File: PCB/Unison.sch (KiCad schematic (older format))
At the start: 258 parts, among them J1 USB4085-GF-A_REVA, U1 ATmega32U4-AU, Y1 16MHz

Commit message: Update: 回路図、PCB。ロータリーエンコーダをマウント穴付きのEC11Kタイプに対応。
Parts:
- SW_RE1, SW_RE2, SW_RE3, SW_RE4, SW_RE5: footprint Rotary_Encoder:RotaryEncoder_Alps_EC11E-Switch_Vertical_H20mm -> ukiha:RotaryEncoder_Alps_EC11K-Switch_Vertical_H20mm
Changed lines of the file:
@@
 F 0 "SW_RE1" H 1150 11267 50  0000 C CNN
 F 1 "Rotary_Encoder_Switch" H 1150 11176 50  0000 C CNN
-F 2 "Rotary_Encoder:RotaryEncoder_Alps_EC11E-Switch_Vertical_H20mm" H 1000 11060 50  0001 C CNN
+F 2 "ukiha:RotaryEncoder_Alps_EC11K-Switch_Vertical_H20mm" H 1000 11060 50  0001 C CNN
 F 3 "~" H 1150 11160 50  0001 C CNN
 	1    1150 10900
@@
 F 0 "SW_RE2" H 2525 11267 50  0000 C CNN
 F 1 "Rotary_Encoder_Switch" H 2525 11176 50  0000 C CNN
-F 2 "Rotary_Encoder:RotaryEncoder_Alps_EC11E-Switch_Vertical_H20mm" H 2375 11060 50  0001 C CNN
+F 2 "ukiha:RotaryEncoder_Alps_EC11K-Switch_Vertical_H20mm" H 2375 11060 50  0001 C CNN
 F 3 "~" H 2525 11160 50  0001 C CNN
 	1    2525 10900
@@
 F 0 "SW_RE3" H 4150 11267 50  0000 C CNN
 F 1 "Rotary_Encoder_Switch" H 4150 11176 50  0000 C CNN
-F 2 "Rotary_Encoder:RotaryEncoder_Alps_EC11E-Switch_Vertical_H20mm" H 4000 11060 50  0001 C CNN
+F 2 "ukiha:RotaryEncoder_Alps_EC11K-Switch_Vertical_H20mm" H 4000 11060 50  0001 C CNN
 F 3 "~" H 4150 11160 50  0001 C CNN
 	1    4150 10900
@@
 F 0 "SW_RE4" H 5550 11267 50  0000 C CNN
 F 1 "Rotary_Encoder_Switch" H 5550 11176 50  0000 C CNN
-F 2 "Rotary_Encoder:RotaryEncoder_Alps_EC11E-Switch_Vertical_H20mm" H 5400 11060 50  0001 C CNN
+F 2 "ukiha:RotaryEncoder_Alps_EC11K-Switch_Vertical_H20mm" H 5400 11060 50  0001 C CNN
 F 3 "~" H 5550 11160 50  0001 C CNN
 	1    5550 10900
@@
 F 0 "SW_RE5" H 6950 11267 50  0000 C CNN
 F 1 "Rotary_Encoder_Switch" H 6950 11176 50  0000 C CNN
-F 2 "Rotary_Encoder:RotaryEncoder_Alps_EC11E-Switch_Vertical_H20mm" H 6800 11060 50  0001 C CNN
+F 2 "ukiha:RotaryEncoder_Alps_EC11K-Switch_Vertical_H20mm" H 6800 11060 50  0001 C CNN
 F 3 "~" H 6950 11160 50  0001 C CNN
 	1    6950 10900

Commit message: Update: ポテンションメータを追加。配線未完了。
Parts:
- added RV1: R_POT, Potentiometer_THT:Potentiometer_Bourns_PTA3043_Single_Slide, symbol Device:R_POT
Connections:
- net +5V: now also RV1.1
- net GND: now also RV1.3
- net AUDIO1 renamed AUDIO
- net AUDIO: no longer U1.30 (PB6)
- new net ANALOG: RV1.2, U1.30 (PB6)
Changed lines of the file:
@@
 $EndComp
 Text GLabel 1450 9925 2    50   Input ~ 0
-AUDIO1
+AUDIO
 $Comp
 L power:GND #PWR01
@@
 Wire Wire Line
 	925  10025 925  10225
-Text GLabel 15300 2725 2    50   Input ~ 0
-AUDIO1
+Text GLabel 15300 3025 2    50   Input ~ 0
+AUDIO
 Connection ~ 4800 6575
 Wire Wire Line
@@
 	1    0    0    -1
 $EndComp
-Text GLabel 15300 3025 2    50   Input ~ 0
-AUDIO2[Reserve]
+Text GLabel 15300 2725 2    50   Input ~ 0
+ANALOG
 Connection ~ 1075 10225
 Wire Wire Line
@@
 Text GLabel 11050 2650 1    50   Input ~ 0
 RE5_2
-Text GLabel 1450 9775 2    50   Input ~ 0
-AUDIO2[Reserve]
-Wire Wire Line
-	1375 9925 1400 9925
-Wire Wire Line
-	1450 9775 1400 9775
-Connection ~ 1400 9925
-Wire Wire Line
-	1400 9925 1450 9925
 $Comp
 L power:GND #PWR029
@@
 	9350 9925 9825 9925
 Wire Wire Line
-	1400 9775 1400 9925
-Wire Wire Line
 	9825 9725 9825 9925
 Connection ~ 9825 9925
@@
 Wire Wire Line
 	10225 4575 10400 4575
+Wire Wire Line
+	1375 9925 1450 9925
+$Comp
+L Device:R_POT RV1
+U 1 1 600D2738
+P 2550 9925
+F 0 "RV1" H 2481 9971 50  0000 R CNN
+F 1 "R_POT" H 2481 9880 50  0000 R CNN
+F 2 "Potentiometer_THT:Potentiometer_Bourns_PTA3043_Single_Slide" H 2550 9925 50  0001 C CNN
+F 3 "~" H 2550 9925 50  0001 C CNN
+	1    2550 9925
+	1    0    0    -1
+$EndComp
+Text GLabel 2700 9925 2    50   Input ~ 0
+ANALOG
+$Comp
+L power:GND #PWR010
+U 1 1 6012B75D
+P 2550 10075
+F 0 "#PWR010" H 2550 9825 50  0001 C CNN
+F 1 "GND" H 2555 9902 50  0000 C CNN
+F 2 "" H 2550 10075 50  0001 C CNN
+F 3 "" H 2550 10075 50  0001 C CNN
+	1    2550 10075
+	1    0    0    -1
+$EndComp
+$Comp
+L power:+5V #PWR09
+U 1 1 60184491
+P 2550 9775
+F 0 "#PWR09" H 2550 9625 50  0001 C CNN
+F 1 "+5V" H 2565 9948 50  0000 C CNN
+F 2 "" H 2550 9775 50  0001 C CNN
+F 3 "" H 2550 9775 50  0001 C CNN
+	1    2550 9775
+	1    0    0    -1
+$EndComp
 $EndSCHEMATC

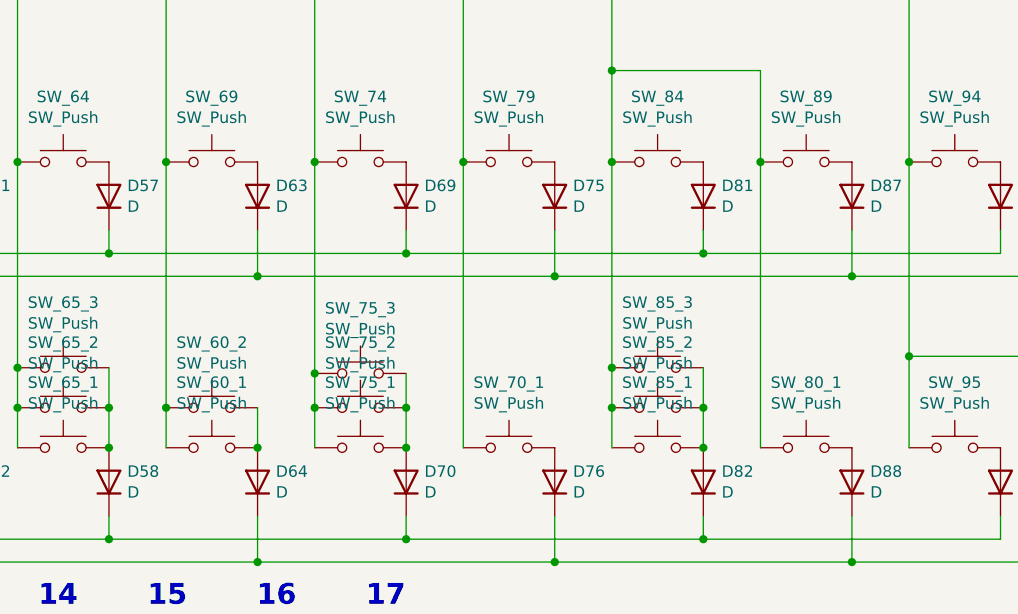
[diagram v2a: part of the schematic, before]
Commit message: Update: 右手親指Modに3キー追加。
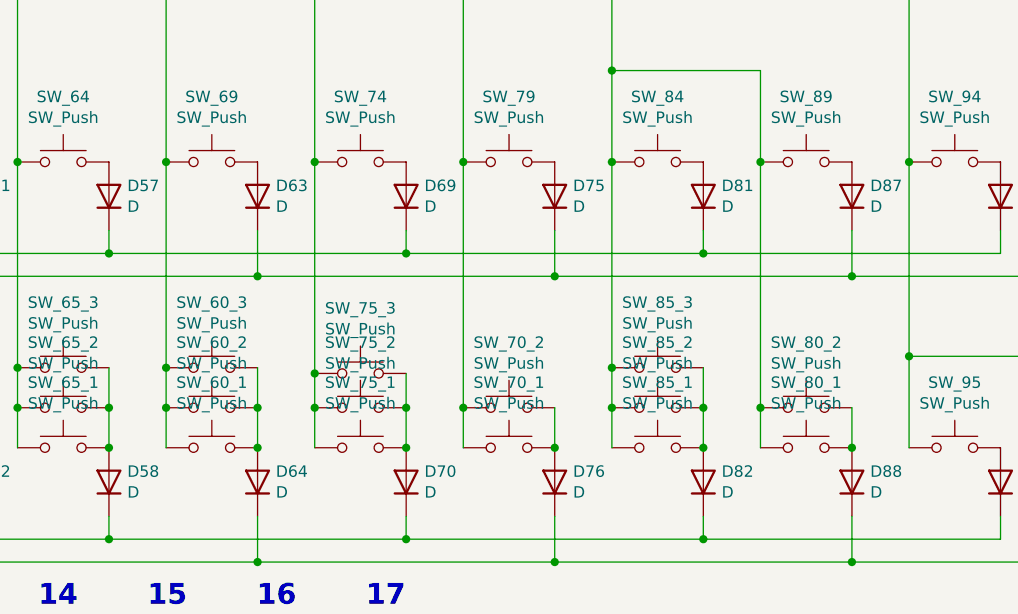
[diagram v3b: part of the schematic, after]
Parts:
- added SW_60_3: SW_Push, ukiha:CherryMX_MidHeight_16mm_rev2_2u_guide, symbol Switch:SW_Push
- added SW_70_2, SW_80_2: SW_Push, ukiha:CherryMX_MidHeight_16mm_rev2_1.5u_guide, symbol Switch:SW_Push
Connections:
- net RE2_1: now also SW_60_3.1
- net RE3_1: now also SW_70_2.1
- net RE4_1: now also SW_80_2.1
- net at D76.2 (A), SW_70_1.2: now also SW_70_2.2
- net at D88.2 (A), SW_80_1.2: now also SW_80_2.2
- net at D64.2 (A), SW_60_1.2, SW_60_2.2: now also SW_60_3.2
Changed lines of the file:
@@
 	4800 7225 4800 7825
 Wire Wire Line
-	7400 6575 7400 7650
+	7400 6575 7400 7475
 Wire Wire Line
 	8050 6575 8050 7500
 Wire Wire Line
-	8700 6575 8700 7825
+	8700 6575 8700 7650
 Wire Wire Line
 	9350 6575 9350 7475
 Wire Wire Line
-	10000 6575 10000 7825
+	10000 6575 10000 7650
 Wire Wire Line
 	2200 6575 2200 7625
@@
 	1    0    0    -1
 $EndComp
+$Comp
+L Switch:SW_Push SW_80_2
+U 1 1 601AB361
+P 10200 7650
+F 0 "SW_80_2" H 10200 7935 50  0000 C CNN
+F 1 "SW_Push" H 10200 7844 50  0000 C CNN
+F 2 "ukiha:CherryMX_MidHeight_16mm_rev2_1.5u_guide" H 10200 7850 50  0001 C CNN
+F 3 "~" H 10200 7850 50  0001 C CNN
+	1    10200 7650
+	1    0    0    -1
+$EndComp
+Connection ~ 10000 7650
+Wire Wire Line
+	10000 7650 10000 7825
+Wire Wire Line
+	10400 7650 10400 7825
+Connection ~ 10400 7825
+$Comp
+L Switch:SW_Push SW_70_2
+U 1 1 6026A20D
+P 8900 7650
+F 0 "SW_70_2" H 8900 7935 50  0000 C CNN
+F 1 "SW_Push" H 8900 7844 50  0000 C CNN
+F 2 "ukiha:CherryMX_MidHeight_16mm_rev2_1.5u_guide" H 8900 7850 50  0001 C CNN
+F 3 "~" H 8900 7850 50  0001 C CNN
+	1    8900 7650
+	1    0    0    -1
+$EndComp
+Connection ~ 8700 7650
+Wire Wire Line
+	8700 7650 8700 7825
+Wire Wire Line
+	9100 7650 9100 7825
+Connection ~ 9100 7825
+$Comp
+L Switch:SW_Push SW_60_3
+U 1 1 6032DF0B
+P 7600 7475
+F 0 "SW_60_3" H 7600 7760 50  0000 C CNN
+F 1 "SW_Push" H 7600 7669 50  0000 C CNN
+F 2 "ukiha:CherryMX_MidHeight_16mm_rev2_2u_guide" H 7600 7675 50  0001 C CNN
+F 3 "~" H 7600 7675 50  0001 C CNN
+	1    7600 7475
+	1    0    0    -1
+$EndComp
+Connection ~ 7400 7475
+Wire Wire Line
+	7400 7475 7400 7650
+Wire Wire Line
+	7800 7475 7800 7650
+Connection ~ 7800 7650
 $EndSCHEMATC

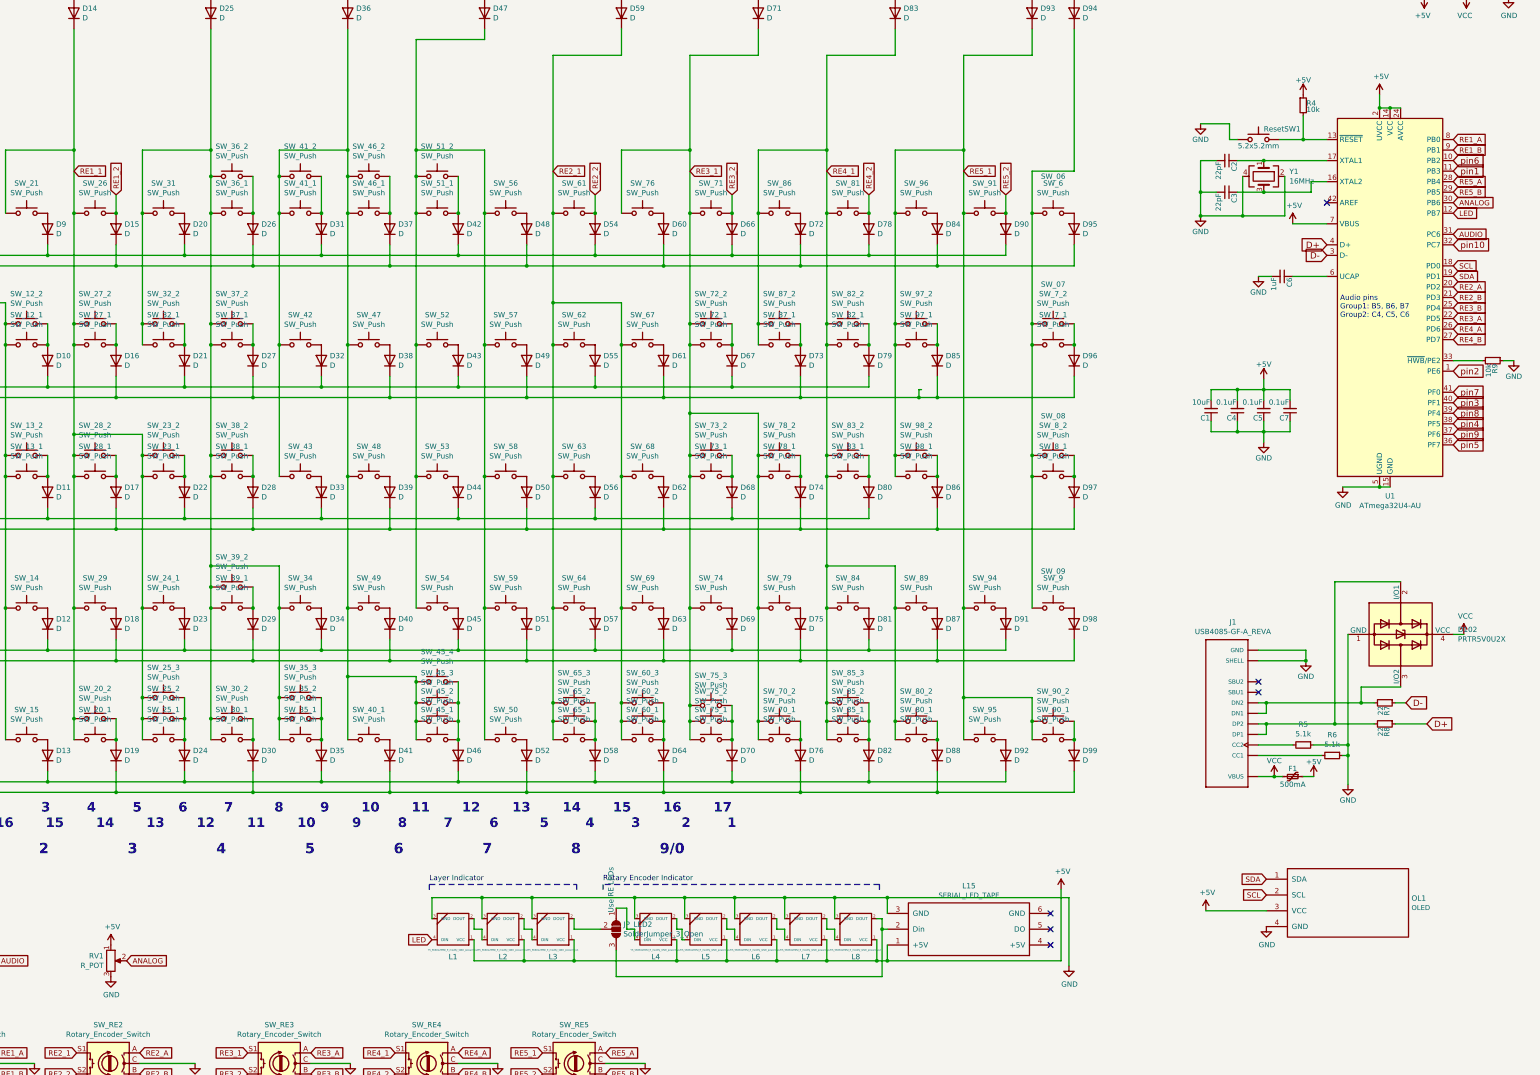
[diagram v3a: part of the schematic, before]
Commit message: Update: OLED, ポテンションメーター廃止。ICSPとI2Cをピンヘッダで用意。
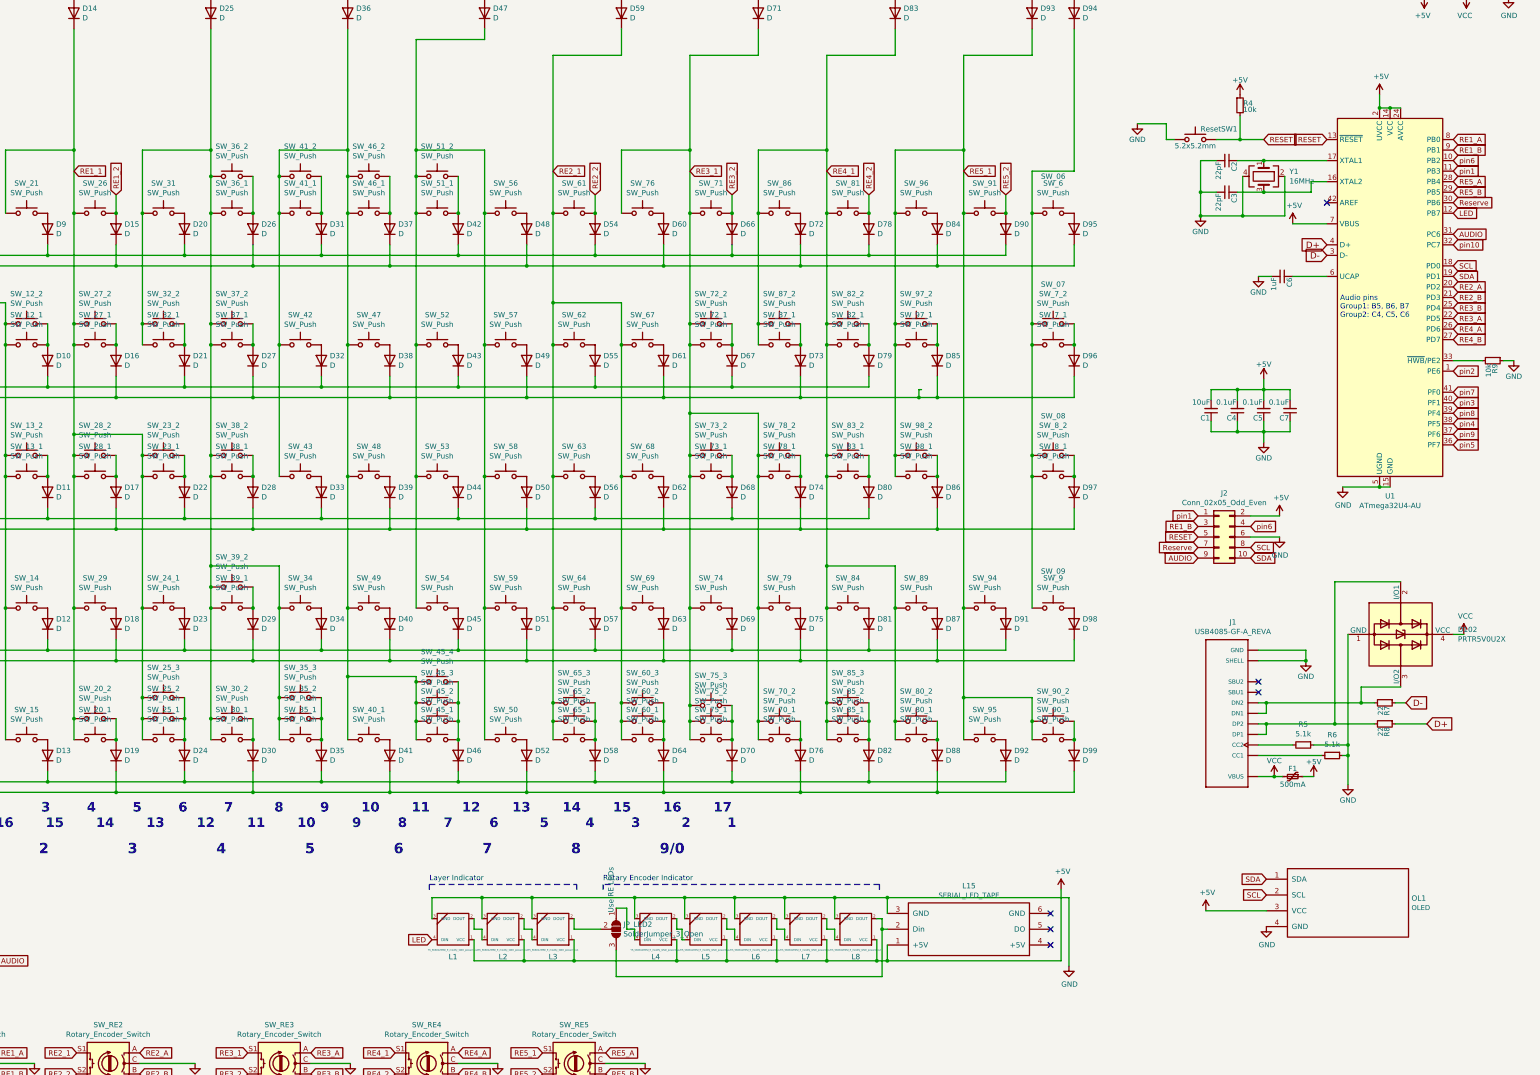
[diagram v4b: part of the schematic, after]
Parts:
- removed RV1: R_POT, Potentiometer_THT:Potentiometer_Bourns_PTA3043_Single_Slide, symbol Device:R_POT
- added J2: Conn_02x05_Odd_Even, Connector_PinHeader_2.54mm:PinHeader_2x05_P2.54mm_Vertical, symbol Connector_Generic:Conn_02x05_Odd_Even
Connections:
- net +5V: now also J2.2 (Pin_2)
- net AUDIO: now also J2.9 (Pin_9)
- net GND: now also J2.6 (Pin_6)
- net RE1_B: now also J2.3 (Pin_3)
- net SCL: now also J2.8 (Pin_8)
- net SDA: now also J2.10 (Pin_10)
- net pin1: now also J2.1 (Pin_1)
- net pin6: now also J2.4 (Pin_4)
- net RESET: now reaches R4.2, ResetSW1.2, U1.13 (~RESET)
- net RESET: now also J2.5 (Pin_5)
- net ANALOG renamed Reserve
- net Reserve: now also J2.7 (Pin_7)
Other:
- moved on the sheet: R4, ResetSW1
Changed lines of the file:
@@
 L Device:R_Small R4
 U 1 1 5B32301F
-P 13875 1800
-F 0 "R4" H 13905 1820 50  0000 L CNN
-F 1 "10k" H 13905 1760 50  0000 L CNN
-F 2 "Resistor_SMD:R_0805_2012Metric_Pad1.20x1.40mm_HandSolder" H 13875 1800 50  0001 C CNN
-F 3 "" H 13875 1800 50  0001 C CNN
-F 4 "C17414" H 13875 1800 50  0001 C CNN "LCSC"
-	1    13875 1800
+P 13275 1800
+F 0 "R4" H 13305 1820 50  0000 L CNN
+F 1 "10k" H 13305 1760 50  0000 L CNN
+F 2 "Resistor_SMD:R_0805_2012Metric_Pad1.20x1.40mm_HandSolder" H 13275 1800 50  0001 C CNN
+F 3 "" H 13275 1800 50  0001 C CNN
+F 4 "C17414" H 13275 1800 50  0001 C CNN "LCSC"
+	1    13275 1800
 	1    0    0    -1
 $EndComp
@@
 L power:+5V #PWR023
 U 1 1 5B32363C
-P 13875 1700
-F 0 "#PWR023" H 13875 1550 50  0001 C CNN
-F 1 "+5V" H 13875 1840 50  0000 C CNN
-F 2 "" H 13875 1700 50  0001 C CNN
-F 3 "" H 13875 1700 50  0001 C CNN
-	1    13875 1700
+P 13275 1700
+F 0 "#PWR023" H 13275 1550 50  0001 C CNN
+F 1 "+5V" H 13275 1840 50  0000 C CNN
+F 2 "" H 13275 1700 50  0001 C CNN
+F 3 "" H 13275 1700 50  0001 C CNN
+	1    13275 1700
 	1    0    0    -1
 $EndComp
@@
 L Jones-rescue:SW_Push ResetSW1
 U 1 1 5B323AA5
-P 13450 2125
-F 0 "ResetSW1" H 13500 2225 50  0000 L CNN
-F 1 "5.2x5.2mm" H 13450 2065 50  0000 C CNN
-F 2 "Button_Switch_SMD:SW_SPST_SKQG_WithStem" H 13450 2325 50  0001 C CNN
-F 3 "" H 13450 2325 50  0001 C CNN
-F 4 "" H 13450 2125 50  0001 C CNN "LCSC"
-	1    13450 2125
+P 12850 2125
+F 0 "ResetSW1" H 12900 2225 50  0000 L CNN
+F 1 "5.2x5.2mm" H 12850 2065 50  0000 C CNN
+F 2 "Button_Switch_SMD:SW_SPST_SKQG_WithStem" H 12850 2325 50  0001 C CNN
+F 3 "" H 12850 2325 50  0001 C CNN
+F 4 "" H 12850 2125 50  0001 C CNN "LCSC"
+	1    12850 2125
 	1    0    0    -1
 $EndComp
@@
 L power:GND #PWR015
 U 1 1 5B323C60
-P 12900 1975
-F 0 "#PWR015" H 12900 1725 50  0001 C CNN
-F 1 "GND" H 12900 1825 50  0000 C CNN
-F 2 "" H 12900 1975 50  0001 C CNN
-F 3 "" H 12900 1975 50  0001 C CNN
-	1    12900 1975
+P 12300 1975
+F 0 "#PWR015" H 12300 1725 50  0001 C CNN
+F 1 "GND" H 12300 1825 50  0000 C CNN
+F 2 "" H 12300 1975 50  0001 C CNN
+F 3 "" H 12300 1975 50  0001 C CNN
+	1    12300 1975
 	1    0    0    -1
 $EndComp
@@
 	-1   0    0    1
 $EndComp
-Text GLabel 15300 2325 2    60   Input ~ 0
+Text GLabel 15300 2325 2    50   Input ~ 0
 pin6
-Text GLabel 15300 5025 2    60   Input ~ 0
+Text GLabel 15300 5025 2    50   Input ~ 0
 pin5
-Text GLabel 15300 4825 2    60   Input ~ 0
+Text GLabel 15300 4825 2    50   Input ~ 0
 pin4
-Text GLabel 15300 4625 2    60   Input ~ 0
+Text GLabel 15300 4625 2    50   Input ~ 0
 pin3
-Text GLabel 15300 4325 2    60   Input ~ 0
+Text GLabel 15300 4325 2    50   Input ~ 0
 pin2
-Text GLabel 15300 2425 2    60   Input ~ 0
+Text GLabel 15300 2425 2    50   Input ~ 0
 pin1
-Text GLabel 15300 3125 2    60   Input ~ 0
+Text GLabel 15300 3125 2    50   Input ~ 0
 pin10
 Wire Wire Line
@@
 	13450 3425 13575 3425
 Wire Wire Line
-	13175 2125 13250 2125
+	12575 2125 12650 2125
 Wire Wire Line
 	13050 2325 12900 2325
@@
 	14100 2925 13775 2925
 Wire Wire Line
-	12900 1975 13175 1975
+	12300 1975 12575 1975
 Wire Wire Line
-	13175 1975 13175 2125
+	12575 1975 12575 2125
 $Comp
 L power:GND #PWR027
@@
 Connection ~ 12900 2850
 Wire Wire Line
-	13650 2125 13875 2125
+	13050 2125 13275 2125
 Wire Wire Line
-	13875 1900 13875 2125
-Connection ~ 13875 2125
+	13275 1900 13275 2125
+Connection ~ 13275 2125
 Wire Wire Line
-	13875 2125 14100 2125
+	13275 2125 13500 2125
 $Comp
 L Device:Crystal_GND24 Y1
@@
 Text GLabel 15300 2825 2    50   Input ~ 0
 LED
-Text GLabel 15300 4925 2    60   Input ~ 0
+Text GLabel 15300 4925 2    50   Input ~ 0
 pin9
-Text GLabel 15300 4725 2    60   Input ~ 0
+Text GLabel 15300 4725 2    50   Input ~ 0
 pin8
-Text GLabel 15300 4525 2    60   Input ~ 0
+Text GLabel 15300 4525 2    50   Input ~ 0
 pin7
 $Comp
@@
 	1    0    0    -1
 $EndComp
-Text GLabel 15300 2725 2    50   Input ~ 0
-ANALOG
 Connection ~ 1075 10225
 Wire Wire Line
@@
 	1375 9925 1450 9925
 $Comp
-L Device:R_POT RV1
-U 1 1 600D2738
-P 2550 9925
-F 0 "RV1" H 2481 9971 50  0000 R CNN
-F 1 "R_POT" H 2481 9880 50  0000 R CNN
-F 2 "Potentiometer_THT:Potentiometer_Bourns_PTA3043_Single_Slide" H 2550 9925 50  0001 C CNN
-F 3 "~" H 2550 9925 50  0001 C CNN
-	1    2550 9925
-	1    0    0    -1
-$EndComp
-Text GLabel 2700 9925 2    50   Input ~ 0
-ANALOG
-$Comp
-L power:GND #PWR010
-U 1 1 6012B75D
-P 2550 10075
-F 0 "#PWR010" H 2550 9825 50  0001 C CNN
-F 1 "GND" H 2555 9902 50  0000 C CNN
-F 2 "" H 2550 10075 50  0001 C CNN
-F 3 "" H 2550 10075 50  0001 C CNN
-	1    2550 10075
-	1    0    0    -1
-$EndComp
-$Comp
-L power:+5V #PWR09
-U 1 1 60184491
-P 2550 9775
-F 0 "#PWR09" H 2550 9625 50  0001 C CNN
-F 1 "+5V" H 2565 9948 50  0000 C CNN
-F 2 "" H 2550 9775 50  0001 C CNN
-F 3 "" H 2550 9775 50  0001 C CNN
-	1    2550 9775
-	1    0    0    -1
-$EndComp
-$Comp
 L Switch:SW_Push SW_80_2
 U 1 1 601AB361
@@
 	7800 7475 7800 7650
 Connection ~ 7800 7650
+$Comp
+L Connector_Generic:Conn_02x05_Odd_Even J2
+U 1 1 604EDB2E
+P 13075 5900
+F 0 "J2" H 13125 6317 50  0000 C CNN
+F 1 "Conn_02x05_Odd_Even" H 13125 6226 50  0000 C CNN
+F 2 "Connector_PinHeader_2.54mm:PinHeader_2x05_P2.54mm_Vertical" H 13075 5900 50  0001 C CNN
+F 3 "~" H 13075 5900 50  0001 C CNN
+	1    13075 5900
+	1    0    0    -1
+$EndComp
+$Comp
+L power:+5V #PWR09
+U 1 1 604F00F6
+P 13650 5700
+F 0 "#PWR09" H 13650 5550 50  0001 C CNN
+F 1 "+5V" H 13665 5873 50  0000 C CNN
+F 2 "" H 13650 5700 50  0001 C CNN
+F 3 "" H 13650 5700 50  0001 C CNN
+	1    13650 5700
+	1    0    0    -1
+$EndComp
+$Comp
+L power:GND #PWR010
+U 1 1 6054A064
+P 13650 5900
+F 0 "#PWR010" H 13650 5650 50  0001 C CNN
+F 1 "GND" H 13655 5727 50  0000 C CNN
+F 2 "" H 13650 5900 50  0001 C CNN
+F 3 "" H 13650 5900 50  0001 C CNN
+	1    13650 5900
+	1    0    0    -1
+$EndComp
+Wire Wire Line
+	13650 5700 13375 5700
+Wire Wire Line
+	13375 5900 13650 5900
+Text GLabel 14100 2125 0    50   Input ~ 0
+RESET
+Text GLabel 13500 2125 2    50   Input ~ 0
+RESET
+Text GLabel 12875 5900 0    50   Input ~ 0
+RESET
+Text GLabel 15300 2725 2    50   Input ~ 0
+Reserve
+Text GLabel 12875 6000 0    50   Input ~ 0
+Reserve
+Text GLabel 13375 6000 2    50   Input ~ 0
+SCL
+Text GLabel 13375 6100 2    50   Input ~ 0
+SDA
+Text GLabel 12875 5700 0    50   Input ~ 0
+pin1
+Text GLabel 13375 5800 2    50   Input ~ 0
+pin6
+Text GLabel 12875 5800 0    50   Input ~ 0
+RE1_B
+Text GLabel 12875 6100 0    50   Input ~ 0
+AUDIO
 $EndSCHEMATC
